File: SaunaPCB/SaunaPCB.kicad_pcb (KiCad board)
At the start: 2 copper layers, 190 x 110 mm, 80 parts, among them J201 KL3RM7.62, J202 KL3RM7.62, J203 KL3RM7.62, J204 KL2RM5.08, J205 KL3RM7.62, J206 KL3RM7.62, J301 KL2RM5.08, J302 KL2RM5.08, J303 KL2RM5.08, J304 KL2RM5.08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

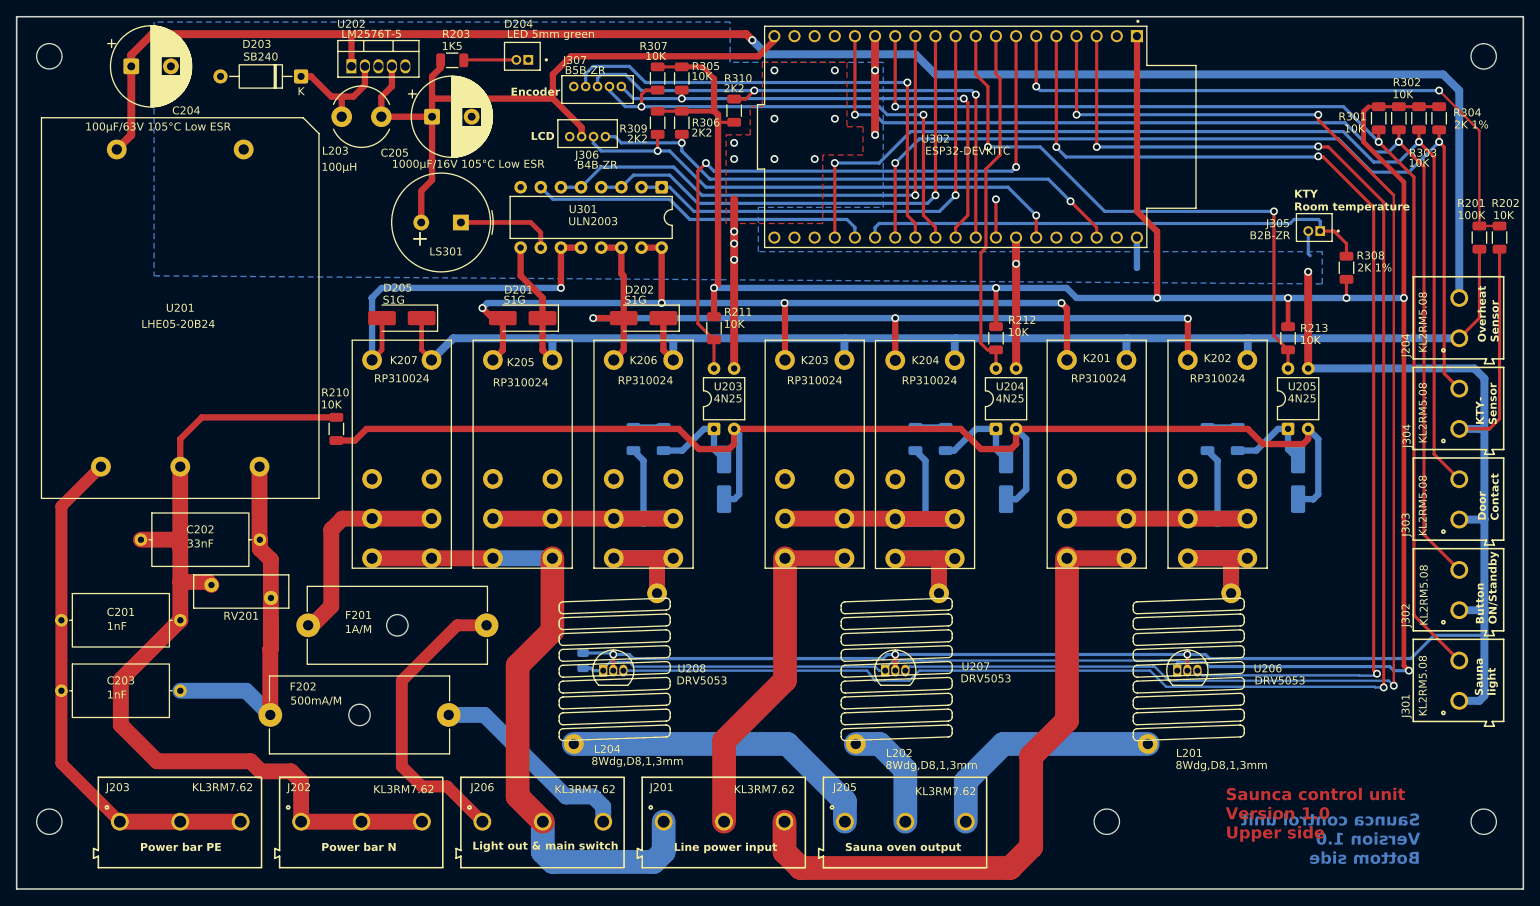
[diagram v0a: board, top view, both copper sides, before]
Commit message: Home brew sensor: Coil and hall sensor combined to one unit to avoid overlap errors on DRC DRC errors removed; 2 warnings left => both acceptable.
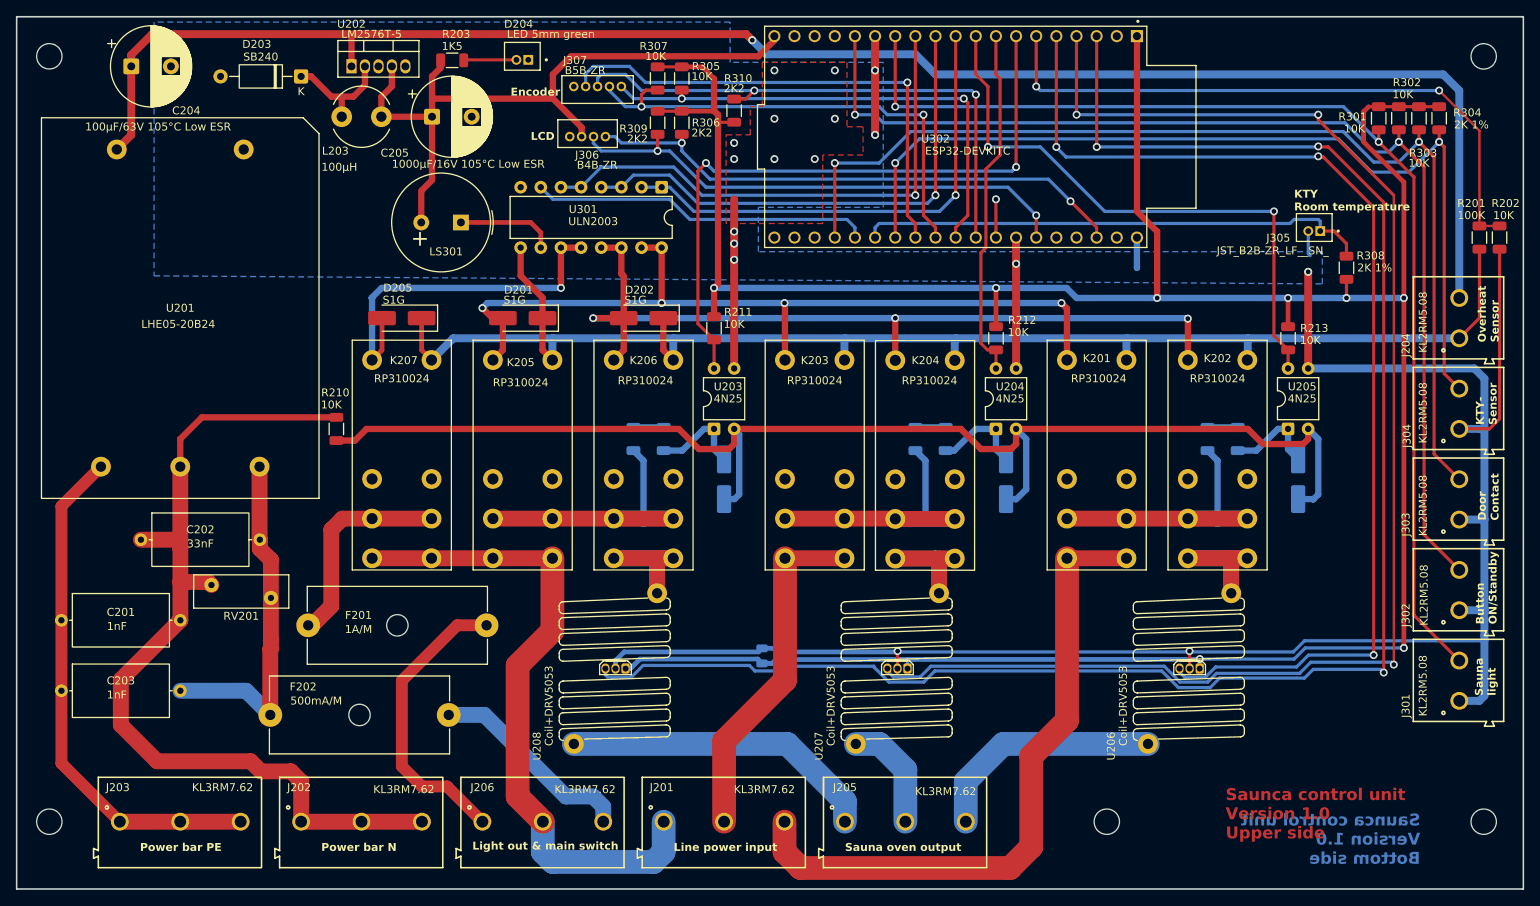
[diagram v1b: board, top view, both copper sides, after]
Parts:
- removed L201, L202, L204: 8Wdg,D8,1,3mm, SaunaProject:Current_Coil_19X14
- J305: value B2B-ZR -> JST_B2B-ZR_LF__SN_
- U206, U207, U208: value DRV5053 -> Coil+DRV5053; footprint Package_TO_SOT_THT:TO-92_Inline -> SaunaProject:Current_Coil_19X14_w_Hall
- moved C206 22.6 mm to (154.0, 127.6)
- moved U206 1.58 mm to (207.9, 129.2), turned to 90 degrees
- moved U208 1.57 mm to (135.5, 129.2), turned to 90 degrees
- moved U207 1.56 mm to (171.1, 129.2), turned to 90 degrees
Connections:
- U206 pad 1: +3V3 -> /Power distribution part/L3_OUT
- U206 pad 2: GND -> /Power distribution part/K202_Out
- U206 pad 3: I_L3 -> +3V3
- U207 pad 1: +3V3 -> /Power distribution part/L2_OUT
- U207 pad 2: GND -> /Power distribution part/K204_Out
- U207 pad 3: I_L2 -> +3V3
- U208 pad 1: +3V3 -> /Power distribution part/L1_OUT
- U208 pad 2: GND -> /Power distribution part/K206_Out
- U208 pad 3: I_L1 -> +3V3
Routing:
- net +3V3: track 370.3 -> 361.4 mm, vias 7 -> 8
- net GND: track 295.1 -> 290.0 mm, vias 18 -> 17
- net I_L1: track 212.2 -> 216.3 mm
- net L1_ON: track 47.1 -> 44.5 mm
- net I_L2: track 179.2 -> 180.7 mm
- net I_L3: track 139.2 -> 140.1 mm

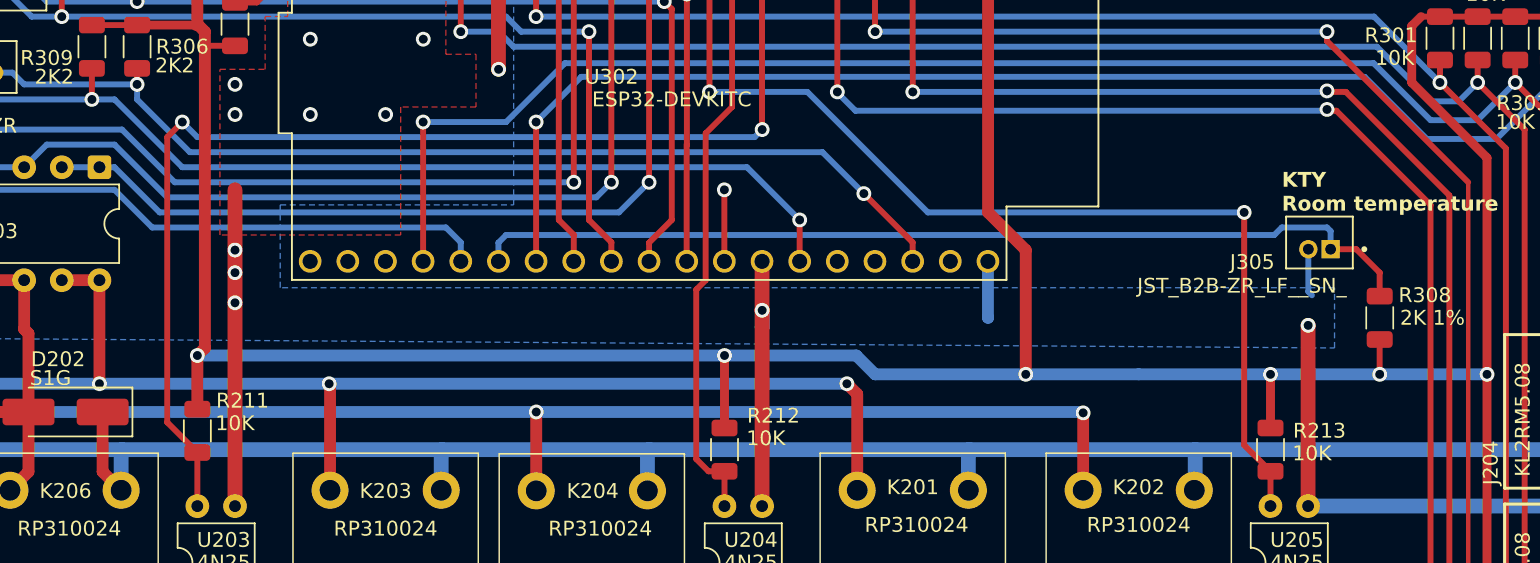
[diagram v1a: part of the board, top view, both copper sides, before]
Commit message: Backlight signal removed two debug pins added remarks regarding KTY added
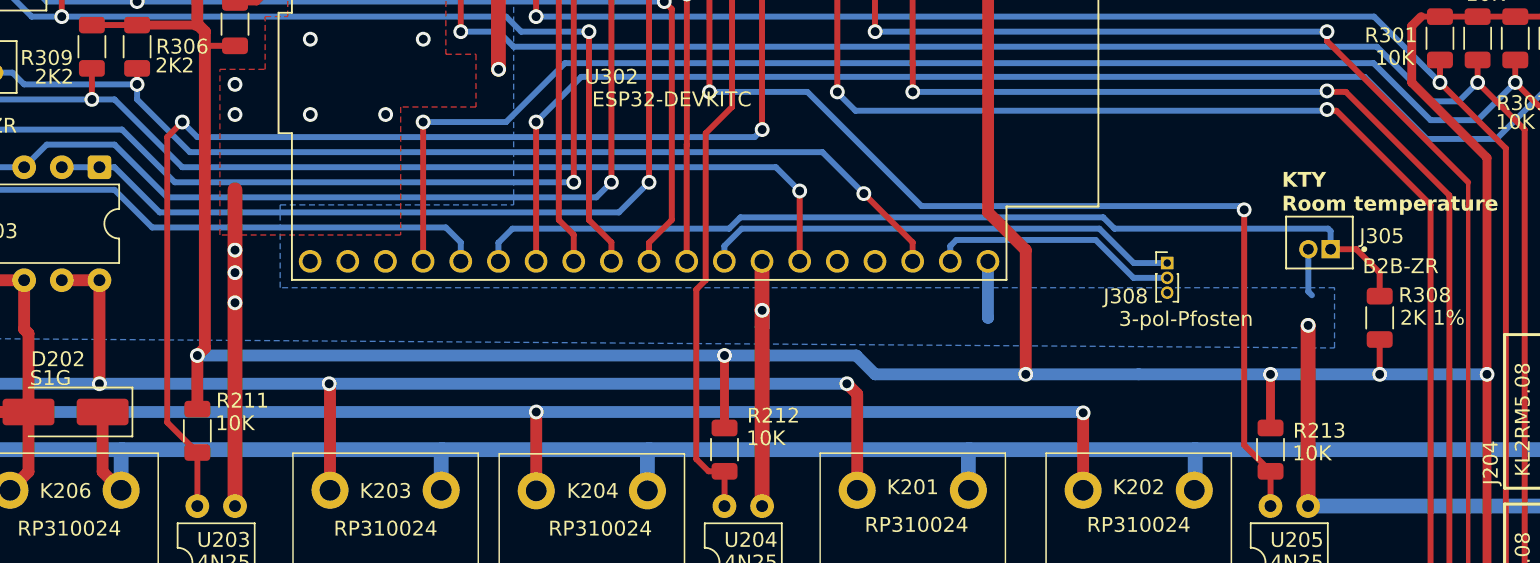
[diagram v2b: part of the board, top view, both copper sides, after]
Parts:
- added J308: 3-pol-Pfosten, Connector_PinHeader_1.00mm:PinHeader_1x03_P1.00mm_Vertical, F.Cu at (213.4, 75.0)
- J305: value JST_B2B-ZR_LF__SN_ -> B2B-ZR
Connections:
- U302 pad 31: /Controller part/LCDBL_3V3 -> /Controller part/Debug_1
- U302 pad 37: unconnected-(U302-IO23-Pad37) -> /Controller part/Debug_2
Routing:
- net /Controller part/Debug_1: track 0.00 -> 32.4 mm
- net /Controller part/Debug_2: track 0.00 -> 16.9 mm
- net /Controller part/LCDBL_3V3: track 4.83 -> 0.00 mm, vias 1 -> 0
- net SDA: track 65.4 -> 66.5 mm
- net KTY_Room: track 64.7 -> 65.3 mm

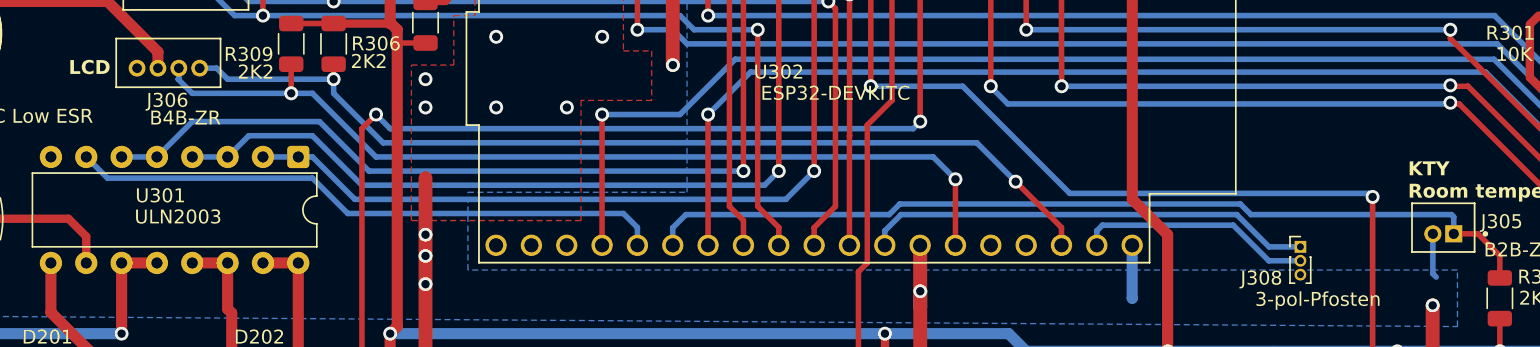
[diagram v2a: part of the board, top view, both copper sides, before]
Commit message: Room KTY moved to IO0 (prior buzzer) Buzzer moved to IO23 (prior Debung_2) Debug_2 removed
Reason IO0 does not work properly as ADC input.
Pretty low input impediance...
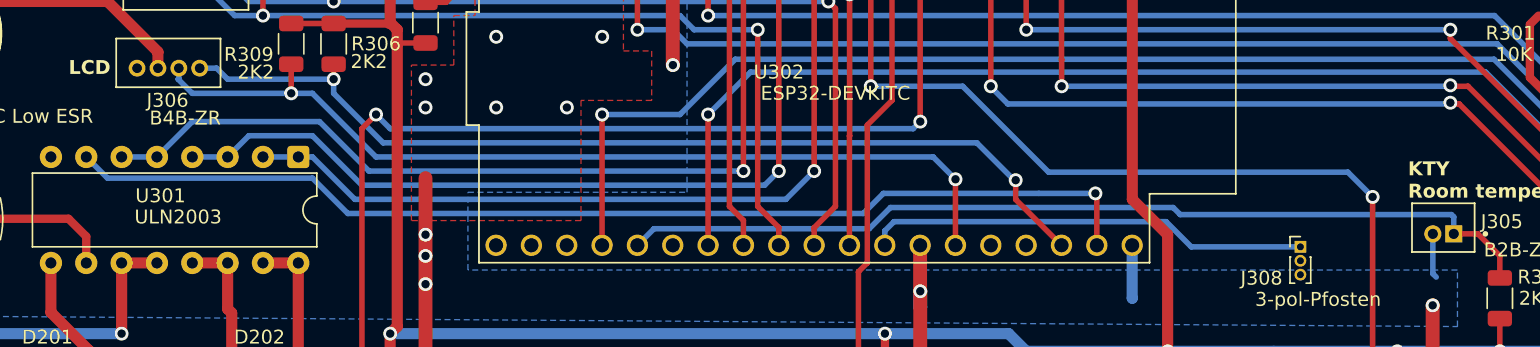
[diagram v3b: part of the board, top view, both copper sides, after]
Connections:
- net /Controller part/Debug_1 renamed /Controller part/Debug
- J308 pad 2: /Controller part/Debug_2 -> unconnected-(J308-Pin_2-Pad2)
- U302 pad 24: /Controller part/Summer_3V3 -> KTY_Room
- U302 pad 25: KTY_Room -> unconnected-(U302-IO0-Pad25)
- U302 pad 37: /Controller part/Debug_2 -> /Controller part/Summer_3V3
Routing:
- net /Controller part/Summer_3V3: track 43.0 -> 78.6 mm, vias 0 -> 1
- net /Controller part/Debug_2: track 16.9 -> 0.00 mm
- net KTY_Room: track 65.3 -> 66.9 mm
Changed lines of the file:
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@@
 	(net 72 "Light_out")
 	(net 73 "unconnected-(U302-SD1-Pad22)")
-	(net 74 "/Controller part/Debug_2")
+	(net 74 "/Controller part/Debug")
 	(net 75 "unconnected-(U302-RXD0-Pad34)")
 	(net 76 "unconnected-(U302-SD2-Pad16)")
@@
 	(net 81 "unconnected-(U302-EN-Pad2)")
 	(net 82 "unconnected-(U302-TXD0-Pad35)")
-	(net 83 "/Controller part/Debug_1")
+	(net 83 "unconnected-(J308-Pin_2-Pad2)")
+	(net 84 "unconnected-(U302-IO0-Pad25)")
 	(footprint "Package_DIP:DIP-4_W7.62mm"
 		(layer "F.Cu")
@@
 			(layers "*.Cu" "*.Mask")
 			(remove_unused_layers no)
-			(net 83 "/Controller part/Debug_1")
+			(net 74 "/Controller part/Debug")
 			(pinfunction "Pin_1")
 			(pintype "passive")
@@
 			(layers "*.Cu" "*.Mask")
 			(remove_unused_layers no)
-			(net 74 "/Controller part/Debug_2")
+			(net 83 "unconnected-(J308-Pin_2-Pad2)")
 			(pinfunction "Pin_2")
-			(pintype "passive")
+			(pintype "passive+no_connect")
 		)
 		(pad "3" thru_hole circle
@@
 			(layers "*.Cu" "*.Mask")
 			(remove_unused_layers no)
-			(net 69 "/Controller part/Summer_3V3")
+			(net 67 "KTY_Room")
 			(pinfunction "IO2")
 			(pintype "bidirectional")
@@
 			(layers "*.Cu" "*.Mask")
 			(remove_unused_layers no)
-			(net 67 "KTY_Room")
+			(net 84 "unconnected-(U302-IO0-Pad25)")
 			(pinfunction "IO0")
-			(pintype "bidirectional")
+			(pintype "bidirectional+no_connect")
 			(solder_mask_margin 0.102)
 		)
@@
 			(layers "*.Cu" "*.Mask")
 			(remove_unused_layers no)
-			(net 83 "/Controller part/Debug_1")
+			(net 74 "/Controller part/Debug")
 			(pinfunction "IO19")
 			(pintype "bidirectional")
@@
 			(layers "*.Cu" "*.Mask")
 			(remove_unused_layers no)
-			(net 74 "/Controller part/Debug_2")
+			(net 69 "/Controller part/Summer_3V3")
 			(pinfunction "IO23")
 			(pintype "bidirectional")
@@
 	)
 	(segment
-		(start 218.298 71.12)
-		(end 196.788 71.12)
+		(start 189.088 63.42)
+		(end 182.484 63.42)
 		(width 0.4)
 		(layer "B.Cu")
@@
 	)
 	(segment
-		(start 196.788 71.12)
+		(start 195.264 69.596)
 		(end 189.088 63.42)
 		(width 0.4)
@@
 	)
 	(segment
-		(start 218.552 71.374)
-		(end 218.298 71.12)
+		(start 216.774 69.596)
+		(end 195.264 69.596)
 		(width 0.4)
 		(layer "B.Cu")
@@
 	)
 	(segment
-		(start 189.088 63.42)
-		(end 182.484 63.42)
+		(start 218.552 71.374)
+		(end 216.774 69.596)
 		(width 0.4)
 		(layer "B.Cu")
@@
 	)
 	(segment
-		(start 192.898 70.278)
-		(end 196.19 73.57)
+		(start 192.898 71.558)
+		(end 192.898 70.17)
 		(width 0.4)
 		(layer "F.Cu")
@@
 	)
 	(segment
-		(start 196.19 73.57)
-		(end 196.19 74.85)
+		(start 196.19 74.85)
+		(end 192.898 71.558)
 		(width 0.4)
 		(layer "F.Cu")
@@
 	)
 	(via
-		(at 192.898 70.278)
+		(at 192.898 70.17)
 		(size 1)
 		(drill 0.6)
@@
 	)
 	(segment
-		(start 143.876 62.912)
-		(end 143.876 63.928)
+		(start 192.79 70.17)
+		(end 192.898 70.17)
 		(width 0.4)
 		(layer "B.Cu")
@@
 	)
 	(segment
-		(start 147.432 67.484)
-		(end 190.104 67.484)
+		(start 190.104 67.484)
+		(end 192.79 70.17)
 		(width 0.4)
 		(layer "B.Cu")
@@
 	)
 	(segment
-		(start 143.876 63.928)
-		(end 147.432 67.484)
+		(start 147.432 67.484)
+		(end 190.104 67.484)
 		(width 0.4)
 		(layer "B.Cu")
@@
 	)
 	(segment
-		(start 190.104 67.484)
-		(end 192.898 70.278)
+		(start 143.876 63.928)
+		(end 147.432 67.484)
 		(width 0.4)
 		(layer "B.Cu")
@@
 	)
 	(segment
+		(start 143.876 62.912)
+		(end 143.876 63.928)
+		(width 0.4)
+		(layer "B.Cu")
+		(net 53)
+	)
+	(segment
 		(start 135.464 62.12)
 		(end 134.248 62.12)
@@
 	)
 	(segment
-		(start 169.196 72.644)
-		(end 183.808058 72.644)
+		(start 224.382 72.806)
+		(end 224.22 72.644)
 		(width 0.4)
 		(layer "B.Cu")
@@
 	)
 	(segment
-		(start 184.570058 71.882)
-		(end 209.042 71.882)
+		(start 183.896 72.136)
+		(end 182.372 73.66)
 		(width 0.4)
 		(layer "B.Cu")
@@
 	)
 	(segment
-		(start 224.382 72.806)
-		(end 224.382 74.03)
+		(start 204.216 72.136)
+		(end 183.896 72.136)
 		(width 0.4)
 		(layer "B.Cu")
@@
 	)
 	(segment
-		(start 224.22 72.644)
+		(start 224.382 74.03)
 		(end 224.382 72.806)
 		(width 0.4)
@@
 	)
 	(segment
-		(start 168.25 73.59)
-		(end 169.196 72.644)
-		(width 0.4)
-		(layer "B.Cu")
-		(net 67)
-	)
-	(segment
-		(start 183.808058 72.644)
-		(end 184.570058 71.882)
+		(start 182.372 73.66)
+		(end 166.9 73.66)
 		(width 0.4)
 		(layer "B.Cu")
@@
 	)
 	(segment
-		(start 209.804 72.644)
-		(end 224.22 72.644)
+		(start 204.724 72.644)
+		(end 204.216 72.136)
 		(width 0.4)
 		(layer "B.Cu")
@@
 	)
 	(segment
-		(start 168.25 74.85)
-		(end 168.25 73.59)
+		(start 224.22 72.644)
+		(end 204.724 72.644)
 		(width 0.4)
 		(layer "B.Cu")
@@
 	)
 	(segment
-		(start 209.042 71.882)
-		(end 209.804 72.644)
+		(start 166.9 73.66)
+		(end 165.71 74.85)
 		(width 0.4)
 		(layer "B.Cu")
@@
 	)
 	(segment
-		(start 142.352 70.024)
-		(end 127.62 70.024)
+		(start 198.73 71.222)
+		(end 198.628 71.12)
 		(width 0.4)
-		(layer "B.Cu")
+		(layer "F.Cu")
 		(net 69)
 	)
 	(segment
-		(start 127.62 70.024)
-		(end 126.096 68.5)
+		(start 198.73 74.85)
+		(end 198.73 71.222)
+		(width 0.4)
+		(layer "F.Cu")
+		(net 69)
+	)
+	(via
+		(at 198.628 71.12)
+		(size 1)
+		(drill 0.6)
+		(layers "F.Cu" "B.Cu")
+		(net 69)
+	)
+	(segment
+		(start 126.096 68.5)
+		(end 127.62 70.024)
 		(width 0.4)
 		(layer "B.Cu")
@@
 	)
 	(segment
-		(start 164.704 72.564)
+		(start 142.352 70.024)
 		(end 144.892 72.564)
 		(width 0.4)
@@
 	)
 	(segment
-		(start 165.71 74.85)
-		(end 165.71 73.57)
+		(start 144.892 72.564)
+		(end 181.944 72.564)
 		(width 0.4)
 		(layer "B.Cu")
@@
 	)
 	(segment
-		(start 165.71 73.57)
-		(end 164.704 72.564)
+		(start 181.944 72.564)
+		(end 183.388 71.12)
 		(width 0.4)
 		(layer "B.Cu")
@@
 	)
 	(segment
-		(start 144.892 72.564)
+		(start 127.62 70.024)
 		(end 142.352 70.024)
 		(width 0.4)
@@
 	)
 	(segment
+		(start 194.564 71.12)
+		(end 198.628 71.12)
+		(width 0.4)
+		(layer "B.Cu")
+		(net 69)
+	)
+	(segment
+		(start 183.388 71.12)
+		(end 194.564 71.12)
+		(width 0.4)
+		(layer "B.Cu")
+		(net 69)
+	)
+	(segment
 		(start 118.984 135.048)
 		(end 114.486 135.048)
@@
 	)
 	(segment
-		(start 211.09 75.962)
-		(end 213.36 75.962)
+		(start 183.49 74.85)
+		(end 183.49 73.812)
 		(width 0.4)
 		(layer "B.Cu")
@@
 	)
 	(segment
-		(start 208.534 73.406)
-		(end 211.09 75.962)
+		(start 205.518 74.962)
+		(end 213.36 74.962)
 		(width 0.4)
 		(layer "B.Cu")
@@
 	)
 	(segment
-		(start 198.73 73.812)
-		(end 199.136 73.406)
+		(start 184.15 73.152)
+		(end 203.708 73.152)
 		(width 0.4)
 		(layer "B.Cu")
@@
 	)
 	(segment
-		(start 199.136 73.406)
-		(end 208.534 73.406)
+		(start 183.49 73.812)
+		(end 184.15 73.152)
 		(width 0.4)
 		(layer "B.Cu")
@@
 	)
 	(segment
-		(start 198.73 74.85)
-		(end 198.73 73.812)
+		(start 203.708 73.152)
+		(end 205.518 74.962)
 		(width 0.4)
 		(layer "B.Cu")
 		(net 74)
 	)
-	(segment
-		(start 183.49 74.85)
-		(end 183.49 73.812)
-		(width 0.4)
-		(layer "B.Cu")
-		(net 83)
-	)
-	(segment
-		(start 183.49 73.812)
-		(end 184.658 72.644)
-		(width 0.4)
-		(layer "B.Cu")
-		(net 83)
-	)
-	(segment
-		(start 211.106 74.962)
-		(end 213.36 74.962)
-		(width 0.4)
-		(layer "B.Cu")
-		(net 83)
-	)
-	(segment
-		(start 208.788 72.644)
-		(end 211.106 74.962)
-		(width 0.4)
-		(layer "B.Cu")
-		(net 83)
-	)
-	(segment
-		(start 184.658 72.644)
-		(end 208.788 72.644)
-		(width 0.4)
-		(layer "B.Cu")
-		(net 83)
-	)
 	(zone
